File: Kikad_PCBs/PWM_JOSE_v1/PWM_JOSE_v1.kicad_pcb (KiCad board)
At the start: 2 copper layers, 197.2 x 153 mm, 528 parts, among them J1 signals, J3 AlimOut, J4 AlimIn, Q1 BC548, Q2 BC558, Q3 Q_NPN_CBE, U1 UC2844N, U2 PC817, U3 TL431

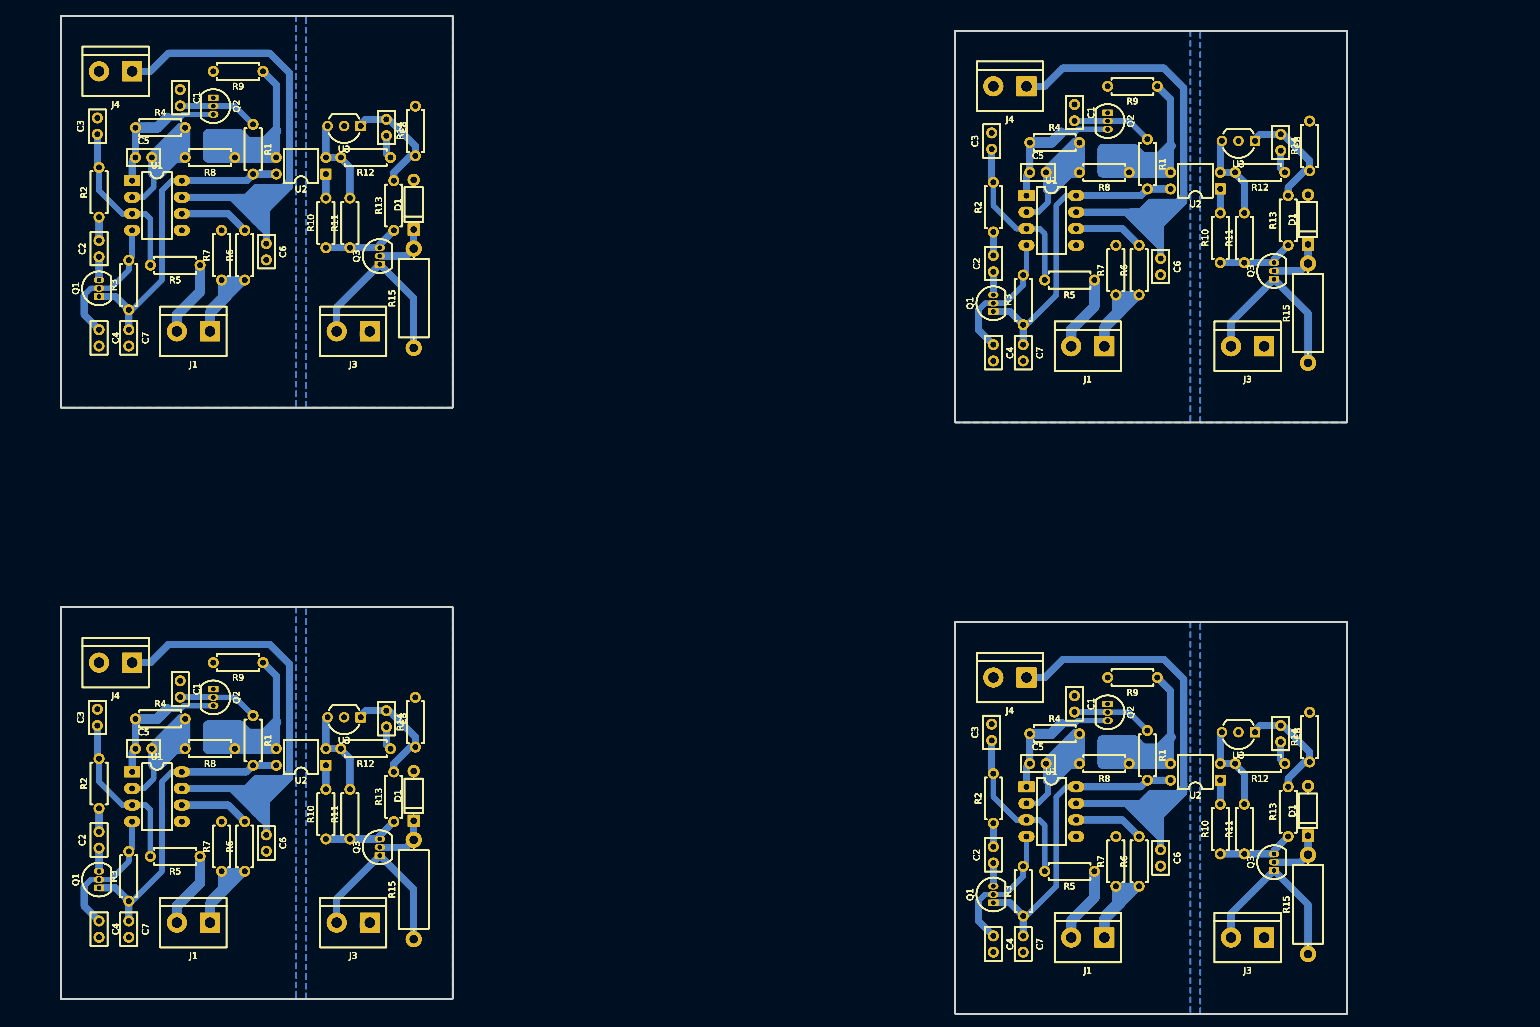
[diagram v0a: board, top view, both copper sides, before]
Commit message: modificacion de serigrafia del PCB y pdf serigrafi
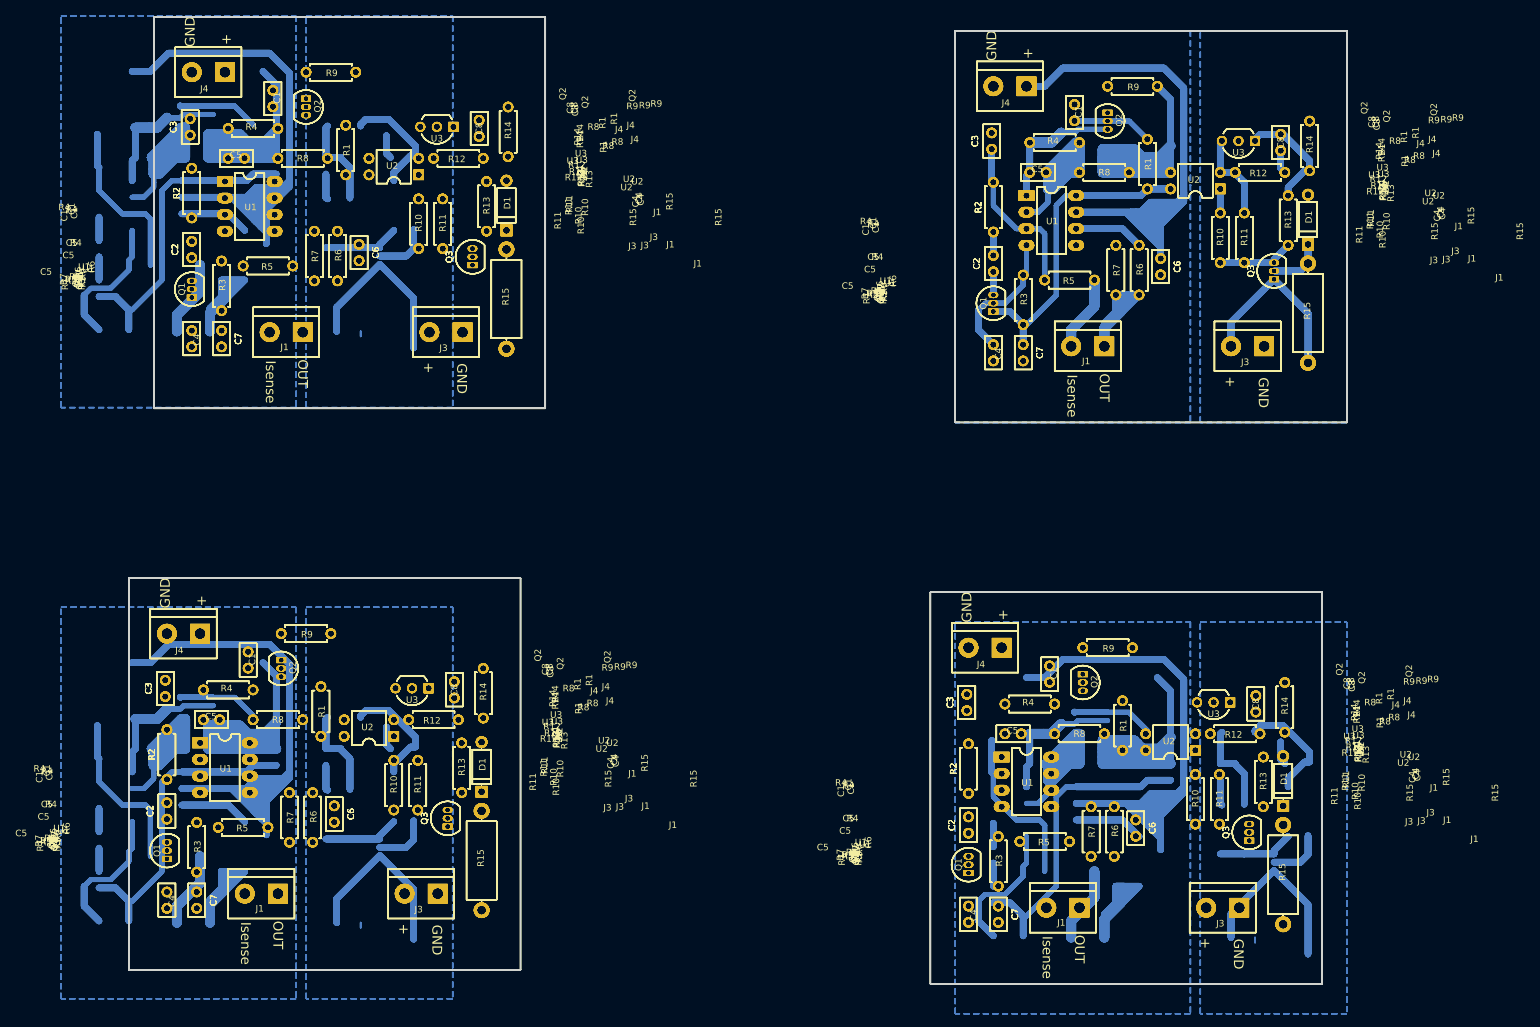
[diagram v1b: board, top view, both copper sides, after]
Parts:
- removed the C1 at (51.3, 126.0) (x4)
- removed the C1 at (51.3, 35.3) (x4)
- removed the C1 at (188.5, 128.3) (x4)
- removed the C2 at (38.9, 151.6) (x4)
- removed the C2 at (38.9, 61.0) (x4)
- removed the C2 at (176.0, 153.9) (x4)
- removed the C3 at (38.6, 132.8) (x4)
- removed the C3 at (38.6, 42.2) (x4)
- removed the C3 at (175.8, 135.1) (x4)
- removed the C4 at (38.9, 162.8) (x4)
- removed the C4 at (38.9, 72.1) (x4)
- removed the C4 at (176.0, 165.1) (x4)
- removed the C5 at (44.5, 136.4) (x4)
- removed the C5 at (44.5, 45.7) (x4)
- removed the C5 at (181.6, 138.7) (x4)
- removed the C6 at (64.5, 149.6) (x4)
- removed the C6 at (64.5, 58.9) (x4)
- removed the C6 at (201.7, 151.9) (x4)
- removed the C7 at (43.4, 162.8) (x4)
- removed the C7 at (43.4, 72.1) (x4)
- removed the C7 at (180.6, 165.1) (x4)
- removed the C8 at (82.9, 130.6) (x4)
- removed the C8 at (82.9, 39.9) (x4)
- removed the C8 at (220.1, 132.8) (x4)
- removed the D1 at (87.1, 147.4) (x4)
- removed the D1 at (87.1, 56.8) (x4)
- removed the D1 at (224.3, 149.7) (x4)
- removed the J1 at (55.9, 163.1) (x4)
- removed the J1 at (55.9, 72.4) (x4)
- removed the J1 at (193.0, 165.4) (x4)
- removed the J3 at (80.4, 163.1) (x4)
- removed the J3 at (80.4, 72.4) (x4)
- removed the J3 at (217.6, 165.4) (x4)
- removed the J4 at (43.9, 123.2) (x4)
- removed the J4 at (43.9, 32.5) (x4)
- removed the J4 at (181.1, 125.5) (x4)
- removed the Q1 at (38.9, 157.7) (x4)
- removed the Q1 at (38.9, 67.1) (x4)
- removed the Q1 at (176.0, 160.0) (x4)
- removed the Q2 at (56.4, 127.3) (x4)
- removed the Q2 at (56.4, 36.6) (x4)
- removed the Q2 at (193.5, 129.5) (x4)
- removed the Q3 at (81.9, 152.8) (x4)
- removed the Q3 at (81.9, 62.1) (x4)
- removed the Q3 at (219.1, 155.1) (x4)
- removed the R1 at (62.5, 131.3) (x4)
- removed the R1 at (62.5, 40.6) (x4)
- removed the R1 at (199.6, 133.6) (x4)
- removed the R10 at (73.7, 150.2) (x4)
- removed the R10 at (73.7, 59.6) (x4)
- removed the R10 at (210.8, 152.5) (x4)
- removed the R11 at (77.3, 150.2) (x4)
- removed the R11 at (77.3, 59.6) (x4)
- removed the R11 at (214.5, 152.5) (x4)
- removed the R12 at (83.6, 136.4) (x4)
- removed the R12 at (83.6, 45.7) (x4)
- removed the R12 at (220.7, 138.7) (x4)
- removed the R13 at (84.1, 147.6) (x4)
- removed the R13 at (84.1, 56.9) (x4)
- removed the R13 at (221.2, 149.9) (x4)
- removed the R14 at (87.4, 136.1) (x4)
- removed the R14 at (87.4, 45.5) (x4)
- removed the R14 at (224.5, 138.4) (x4)
- removed the R15 at (87.1, 165.6) (x4)
- removed the R15 at (87.1, 74.9) (x4)
- removed the R15 at (224.3, 167.9) (x4)
- removed the R2 at (38.9, 145.5) (x4)
- removed the R2 at (38.9, 54.9) (x4)
- removed the R2 at (176.0, 147.8) (x4)
- removed the R3 at (43.4, 159.8) (x4)
- removed the R3 at (43.4, 69.1) (x4)
- removed the R3 at (180.6, 162.1) (x4)
- removed the R4 at (44.5, 131.8) (x4)
- removed the R4 at (44.5, 41.1) (x4)
- removed the R4 at (181.6, 134.1) (x4)
- removed the R5 at (54.4, 152.9) (x4)
- removed the R5 at (54.4, 62.2) (x4)
- removed the R5 at (191.5, 155.2) (x4)
- removed the R6 at (61.2, 155.2) (x4)
- removed the R6 at (61.2, 64.5) (x4)
- removed the R6 at (198.4, 157.5) (x4)
- removed the R7 at (57.7, 155.2) (x4)
- removed the R7 at (57.7, 64.5) (x4)
- removed the R7 at (194.8, 157.5) (x4)
- removed the R8 at (59.7, 136.4) (x4)
- removed the R8 at (59.7, 45.7) (x4)
- removed the R8 at (196.8, 138.7) (x4)
- removed the R9 at (64.0, 123.2) (x4)
- removed the R9 at (64.0, 32.5) (x4)
- removed the R9 at (201.2, 125.5) (x4)
- removed the U1 at (43.9, 140.0) (x4)
- removed the U1 at (43.9, 49.3) (x4)
- removed the U1 at (181.1, 142.2) (x4)
- removed the U2 at (73.7, 138.9) (x4)
- removed the U2 at (73.7, 48.3) (x4)
- removed the U2 at (210.8, 141.2) (x4)
- removed the U3 at (79.0, 131.6) (x4)
- removed the U3 at (79.0, 40.9) (x4)
- removed the U3 at (216.2, 133.9) (x4)
- added C1 (x4): Css, Capacitors_THT:C_Disc_D5.0mm_W2.5mm_P2.50mm, F.Cu at (65.5, 35.4)
- added C1 (x4): Css, Capacitors_THT:C_Disc_D5.0mm_W2.5mm_P2.50mm, F.Cu at (184.7, 123.7)
- added C1 (x4): Css, Capacitors_THT:C_Disc_D5.0mm_W2.5mm_P2.50mm, F.Cu at (61.7, 121.5)
- added C2 (x4): Cramp, Capacitors_THT:C_Disc_D5.0mm_W2.5mm_P2.50mm, F.Cu at (53.1, 61.1)
- added C2 (x4): Cramp, Capacitors_THT:C_Disc_D5.0mm_W2.5mm_P2.50mm, F.Cu at (172.2, 149.4)
- added C2 (x4): Cramp, Capacitors_THT:C_Disc_D5.0mm_W2.5mm_P2.50mm, F.Cu at (49.3, 147.2)
- added C3 (x4): Ccsf, Capacitors_THT:C_Disc_D5.0mm_W2.5mm_P2.50mm, F.Cu at (52.8, 42.3)
- added C3 (x4): Ccsf, Capacitors_THT:C_Disc_D5.0mm_W2.5mm_P2.50mm, F.Cu at (172.0, 130.6)
- added C3 (x4): Ccsf, Capacitors_THT:C_Disc_D5.0mm_W2.5mm_P2.50mm, F.Cu at (49.0, 128.4)
- added C4 (x4): Cct, Capacitors_THT:C_Disc_D5.0mm_W2.5mm_P2.50mm, F.Cu at (53.1, 72.3)
- added C4 (x4): Cct, Capacitors_THT:C_Disc_D5.0mm_W2.5mm_P2.50mm, F.Cu at (172.2, 160.5)
- added C4 (x4): Cct, Capacitors_THT:C_Disc_D5.0mm_W2.5mm_P2.50mm, F.Cu at (49.3, 158.4)
- added C5 (x4): CcmpP, Capacitors_THT:C_Disc_D5.0mm_W2.5mm_P2.50mm, F.Cu at (58.7, 45.8)
- added C5 (x4): CcmpP, Capacitors_THT:C_Disc_D5.0mm_W2.5mm_P2.50mm, F.Cu at (177.8, 134.1)
- added C5 (x4): CcmpP, Capacitors_THT:C_Disc_D5.0mm_W2.5mm_P2.50mm, F.Cu at (54.9, 132.0)
- added C6 (x4): Cvcc, Capacitors_THT:C_Disc_D5.0mm_W2.5mm_P2.50mm, F.Cu at (78.7, 59.1)
- added C6 (x4): Cvcc, Capacitors_THT:C_Disc_D5.0mm_W2.5mm_P2.50mm, F.Cu at (197.9, 147.3)
- added C6 (x4): Cvcc, Capacitors_THT:C_Disc_D5.0mm_W2.5mm_P2.50mm, F.Cu at (74.9, 145.2)
- added C7 (x4): Cvref, Capacitors_THT:C_Disc_D5.0mm_W2.5mm_P2.50mm, F.Cu at (57.7, 72.3)
- added C7 (x4): Cvref, Capacitors_THT:C_Disc_D5.0mm_W2.5mm_P2.50mm, F.Cu at (176.8, 160.5)
- added C7 (x4): Cvref, Capacitors_THT:C_Disc_D5.0mm_W2.5mm_P2.50mm, F.Cu at (53.8, 158.4)
- added C8 (x4): CcmpZ, Capacitors_THT:C_Disc_D5.0mm_W2.5mm_P2.50mm, F.Cu at (97.2, 40.0)
- added C8 (x4): CcmpZ, Capacitors_THT:C_Disc_D5.0mm_W2.5mm_P2.50mm, F.Cu at (216.3, 128.3)
- added C8 (x4): CcmpZ, Capacitors_THT:C_Disc_D5.0mm_W2.5mm_P2.50mm, F.Cu at (93.3, 126.1)
- added D1 (x4): Zener, Diodes_THT:D_A-405_P7.62mm_Horizontal, F.Cu at (101.3, 56.9)
- added D1 (x4): Zener, Diodes_THT:D_A-405_P7.62mm_Horizontal, F.Cu at (220.5, 145.2)
- added D1 (x4): Zener, Diodes_THT:D_A-405_P7.62mm_Horizontal, F.Cu at (97.5, 143.0)
- added J1 (x4): signals, Connectors:bornier2, F.Cu at (70.1, 72.5)
- added J1 (x4): signals, Connectors:bornier2, F.Cu at (189.2, 160.8)
- added J1 (x4): signals, Connectors:bornier2, F.Cu at (66.3, 158.6)
- added J3 (x4): AlimOut, Connectors:bornier2, F.Cu at (94.6, 72.5)
- added J3 (x4): AlimOut, Connectors:bornier2, F.Cu at (213.7, 160.8)
- added J3 (x4): AlimOut, Connectors:bornier2, F.Cu at (90.8, 158.6)
- added J4 (x4): AlimIn, Connectors:bornier2, F.Cu at (58.2, 32.6)
- added J4 (x4): AlimIn, Connectors:bornier2, F.Cu at (177.3, 120.9)
- added J4 (x4): AlimIn, Connectors:bornier2, F.Cu at (54.4, 118.7)
- added Q1 (x4): BC548, TO_SOT_Packages_THT:TO-92_Inline_Narrow_Oval, F.Cu at (53.1, 67.2)
- added Q1 (x4): BC548, TO_SOT_Packages_THT:TO-92_Inline_Narrow_Oval, F.Cu at (172.2, 155.4)
- added Q1 (x4): BC548, TO_SOT_Packages_THT:TO-92_Inline_Narrow_Oval, F.Cu at (49.3, 153.3)
- added Q2 (x4): BC558, TO_SOT_Packages_THT:TO-92_Inline_Narrow_Oval, F.Cu at (70.6, 36.7)
- added Q2 (x4): BC558, TO_SOT_Packages_THT:TO-92_Inline_Narrow_Oval, F.Cu at (189.7, 125.0)
- added Q2 (x4): BC558, TO_SOT_Packages_THT:TO-92_Inline_Narrow_Oval, F.Cu at (66.8, 122.8)
- added Q3 (x4): Q_NPN_CBE, TO_SOT_Packages_THT:TO-92_Inline_Narrow_Oval, F.Cu at (96.1, 62.2)
- added Q3 (x4): Q_NPN_CBE, TO_SOT_Packages_THT:TO-92_Inline_Narrow_Oval, F.Cu at (215.3, 150.5)
- added Q3 (x4): Q_NPN_CBE, TO_SOT_Packages_THT:TO-92_Inline_Narrow_Oval, F.Cu at (92.3, 148.3)
- added R1 (x4): Rss, Resistors_THT:R_Axial_DIN0207_L6.3mm_D2.5mm_P7.62mm_Horizontal, F.Cu at (76.7, 40.8)
- added R1 (x4): Rss, Resistors_THT:R_Axial_DIN0207_L6.3mm_D2.5mm_P7.62mm_Horizontal, F.Cu at (195.8, 129.0)
- added R1 (x4): Rss, Resistors_THT:R_Axial_DIN0207_L6.3mm_D2.5mm_P7.62mm_Horizontal, F.Cu at (72.9, 126.9)
- added R10 (x4): Rled, Resistors_THT:R_Axial_DIN0207_L6.3mm_D2.5mm_P7.62mm_Horizontal, F.Cu at (87.9, 59.7)
- added R10 (x4): Rled, Resistors_THT:R_Axial_DIN0207_L6.3mm_D2.5mm_P7.62mm_Horizontal, F.Cu at (207.0, 148.0)
- added R10 (x4): Rled, Resistors_THT:R_Axial_DIN0207_L6.3mm_D2.5mm_P7.62mm_Horizontal, F.Cu at (84.1, 145.8)
- added R11 (x4): Rbias, Resistors_THT:R_Axial_DIN0207_L6.3mm_D2.5mm_P7.62mm_Horizontal, F.Cu at (91.6, 59.7)
- added R11 (x4): Rbias, Resistors_THT:R_Axial_DIN0207_L6.3mm_D2.5mm_P7.62mm_Horizontal, F.Cu at (210.7, 148.0)
- added R11 (x4): Rbias, Resistors_THT:R_Axial_DIN0207_L6.3mm_D2.5mm_P7.62mm_Horizontal, F.Cu at (87.8, 145.8)
- added R12 (x4): RcmpZ, Resistors_THT:R_Axial_DIN0207_L6.3mm_D2.5mm_P7.62mm_Horizontal, F.Cu at (97.8, 45.8)
- added R12 (x4): RcmpZ, Resistors_THT:R_Axial_DIN0207_L6.3mm_D2.5mm_P7.62mm_Horizontal, F.Cu at (216.9, 134.1)
- added R12 (x4): RcmpZ, Resistors_THT:R_Axial_DIN0207_L6.3mm_D2.5mm_P7.62mm_Horizontal, F.Cu at (94.0, 132.0)
- added R13 (x4): Rfbu, Resistors_THT:R_Axial_DIN0207_L6.3mm_D2.5mm_P7.62mm_Horizontal, F.Cu at (98.3, 57.0)
- added R13 (x4): Rfbu, Resistors_THT:R_Axial_DIN0207_L6.3mm_D2.5mm_P7.62mm_Horizontal, F.Cu at (217.4, 145.3)
- added R13 (x4): Rfbu, Resistors_THT:R_Axial_DIN0207_L6.3mm_D2.5mm_P7.62mm_Horizontal, F.Cu at (94.5, 143.1)
- added R14 (x4): Rfbb, Resistors_THT:R_Axial_DIN0207_L6.3mm_D2.5mm_P7.62mm_Horizontal, F.Cu at (101.6, 45.6)
- added R14 (x4): Rfbb, Resistors_THT:R_Axial_DIN0207_L6.3mm_D2.5mm_P7.62mm_Horizontal, F.Cu at (220.7, 133.9)
- added R14 (x4): Rfbb, Resistors_THT:R_Axial_DIN0207_L6.3mm_D2.5mm_P7.62mm_Horizontal, F.Cu at (97.8, 131.7)
- added R15 (x4): RZ, Resistors_THT:R_Axial_DIN0414_L11.9mm_D4.5mm_P15.24mm_Horizontal, F.Cu at (101.3, 75.1)
- added R15 (x4): RZ, Resistors_THT:R_Axial_DIN0414_L11.9mm_D4.5mm_P15.24mm_Horizontal, F.Cu at (220.5, 163.3)
- added R15 (x4): RZ, Resistors_THT:R_Axial_DIN0414_L11.9mm_D4.5mm_P15.24mm_Horizontal, F.Cu at (97.5, 161.2)
- added R2 (x4): Rramp, Resistors_THT:R_Axial_DIN0207_L6.3mm_D2.5mm_P7.62mm_Horizontal, F.Cu at (53.1, 55.0)
- added R2 (x4): Rramp, Resistors_THT:R_Axial_DIN0207_L6.3mm_D2.5mm_P7.62mm_Horizontal, F.Cu at (172.2, 143.3)
- added R2 (x4): Rramp, Resistors_THT:R_Axial_DIN0207_L6.3mm_D2.5mm_P7.62mm_Horizontal, F.Cu at (49.3, 141.1)
- added R3 (x4): Rrt, Resistors_THT:R_Axial_DIN0207_L6.3mm_D2.5mm_P7.62mm_Horizontal, F.Cu at (57.7, 69.2)
- added R3 (x4): Rrt, Resistors_THT:R_Axial_DIN0207_L6.3mm_D2.5mm_P7.62mm_Horizontal, F.Cu at (176.8, 157.5)
- added R3 (x4): Rrt, Resistors_THT:R_Axial_DIN0207_L6.3mm_D2.5mm_P7.62mm_Horizontal, F.Cu at (53.8, 155.3)
- added R4 (x4): RcmpP, Resistors_THT:R_Axial_DIN0207_L6.3mm_D2.5mm_P7.62mm_Horizontal, F.Cu at (58.7, 41.3)
- added R4 (x4): RcmpP, Resistors_THT:R_Axial_DIN0207_L6.3mm_D2.5mm_P7.62mm_Horizontal, F.Cu at (177.8, 129.5)
- added R4 (x4): RcmpP, Resistors_THT:R_Axial_DIN0207_L6.3mm_D2.5mm_P7.62mm_Horizontal, F.Cu at (54.9, 127.4)
- added R5 (x4): Rcsf, Resistors_THT:R_Axial_DIN0207_L6.3mm_D2.5mm_P7.62mm_Horizontal, F.Cu at (68.6, 62.4)
- added R5 (x4): Rcsf, Resistors_THT:R_Axial_DIN0207_L6.3mm_D2.5mm_P7.62mm_Horizontal, F.Cu at (187.7, 150.6)
- added R5 (x4): Rcsf, Resistors_THT:R_Axial_DIN0207_L6.3mm_D2.5mm_P7.62mm_Horizontal, F.Cu at (64.8, 148.5)
- added R6 (x4): Rg, Resistors_THT:R_Axial_DIN0207_L6.3mm_D2.5mm_P7.62mm_Horizontal, F.Cu at (75.4, 64.6)
- added R6 (x4): Rg, Resistors_THT:R_Axial_DIN0207_L6.3mm_D2.5mm_P7.62mm_Horizontal, F.Cu at (194.6, 152.9)
- added R6 (x4): Rg, Resistors_THT:R_Axial_DIN0207_L6.3mm_D2.5mm_P7.62mm_Horizontal, F.Cu at (71.6, 150.7)
- added R7 (x4): Rbled, Resistors_THT:R_Axial_DIN0207_L6.3mm_D2.5mm_P7.62mm_Horizontal, F.Cu at (71.9, 64.6)
- added R7 (x4): Rbled, Resistors_THT:R_Axial_DIN0207_L6.3mm_D2.5mm_P7.62mm_Horizontal, F.Cu at (191.0, 152.9)
- added R7 (x4): Rbled, Resistors_THT:R_Axial_DIN0207_L6.3mm_D2.5mm_P7.62mm_Horizontal, F.Cu at (68.1, 150.7)
- added R8 (x4): Rfbg, Resistors_THT:R_Axial_DIN0207_L6.3mm_D2.5mm_P7.62mm_Horizontal, F.Cu at (73.9, 45.8)
- added R8 (x4): Rfbg, Resistors_THT:R_Axial_DIN0207_L6.3mm_D2.5mm_P7.62mm_Horizontal, F.Cu at (193.0, 134.1)
- added R8 (x4): Rfbg, Resistors_THT:R_Axial_DIN0207_L6.3mm_D2.5mm_P7.62mm_Horizontal, F.Cu at (70.1, 132.0)
- added R9 (x4): Ropto, Resistors_THT:R_Axial_DIN0207_L6.3mm_D2.5mm_P7.62mm_Horizontal, F.Cu at (78.2, 32.6)
- added R9 (x4): Ropto, Resistors_THT:R_Axial_DIN0207_L6.3mm_D2.5mm_P7.62mm_Horizontal, F.Cu at (197.4, 120.9)
- added R9 (x4): Ropto, Resistors_THT:R_Axial_DIN0207_L6.3mm_D2.5mm_P7.62mm_Horizontal, F.Cu at (74.4, 118.7)
- added U1 (x4): UC2844N, Housings_DIP:DIP-8_W7.62mm_LongPads, F.Cu at (58.2, 49.4)
- added U1 (x4): UC2844N, Housings_DIP:DIP-8_W7.62mm_LongPads, F.Cu at (177.3, 137.7)
- added U1 (x4): UC2844N, Housings_DIP:DIP-8_W7.62mm_LongPads, F.Cu at (54.4, 135.5)
- added U2 (x4): PC817, Housings_DIP:DIP-4_W7.62mm, F.Cu at (87.9, 48.4)
- added U2 (x4): PC817, Housings_DIP:DIP-4_W7.62mm, F.Cu at (207.0, 136.7)
- added U2 (x4): PC817, Housings_DIP:DIP-4_W7.62mm, F.Cu at (84.1, 134.5)
- added U3 (x4): TL431, TO_SOT_Packages_THT:TO-92_Inline_Wide, F.Cu at (93.2, 41.0)
- added U3 (x4): TL431, TO_SOT_Packages_THT:TO-92_Inline_Wide, F.Cu at (212.3, 129.3)
- added U3 (x4): TL431, TO_SOT_Packages_THT:TO-92_Inline_Wide, F.Cu at (89.4, 127.1)
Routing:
- net (no net): track 0.00 -> 3579.9 mm
- net +12V: track 1737.9 -> 805.8 mm
- net Net-(R8-Pad1): track 987.2 -> 370.0 mm
- net Net-(C4-Pad1): track 624.7 -> 156.2 mm
- net GNDREF: track 0.00 -> 399.4 mm
- net Net-(J1-Pad1): track 470.9 -> 117.7 mm
- net +VDC: track 448.1 -> 112.0 mm
- net Net-(C5-Pad1): track 360.9 -> 90.2 mm
- net Net-(C7-Pad1): track 1024.7 -> 764.0 mm
- net Net-(C8-Pad1): track 284.5 -> 71.1 mm
- net Net-(C1-Pad2): track 262.6 -> 65.7 mm
- net Net-(C3-Pad1): track 550.8 -> 367.1 mm
- net Net-(C5-Pad2): track 631.6 -> 757.7 mm
- net GNDS: track 12.2 -> 129.5 mm
- net Net-(Q3-Pad3): track 189.1 -> 81.7 mm
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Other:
- board size 197.2 x 153 mm -> 186.8 x 148.3 mm
- board text added: "+"
- board text added: "GND"
- board text added: "Isense"
- board text added: "OUT"

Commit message: ultimo PCB con las serigrafias V2 (el qeu implemente y funcionaba)
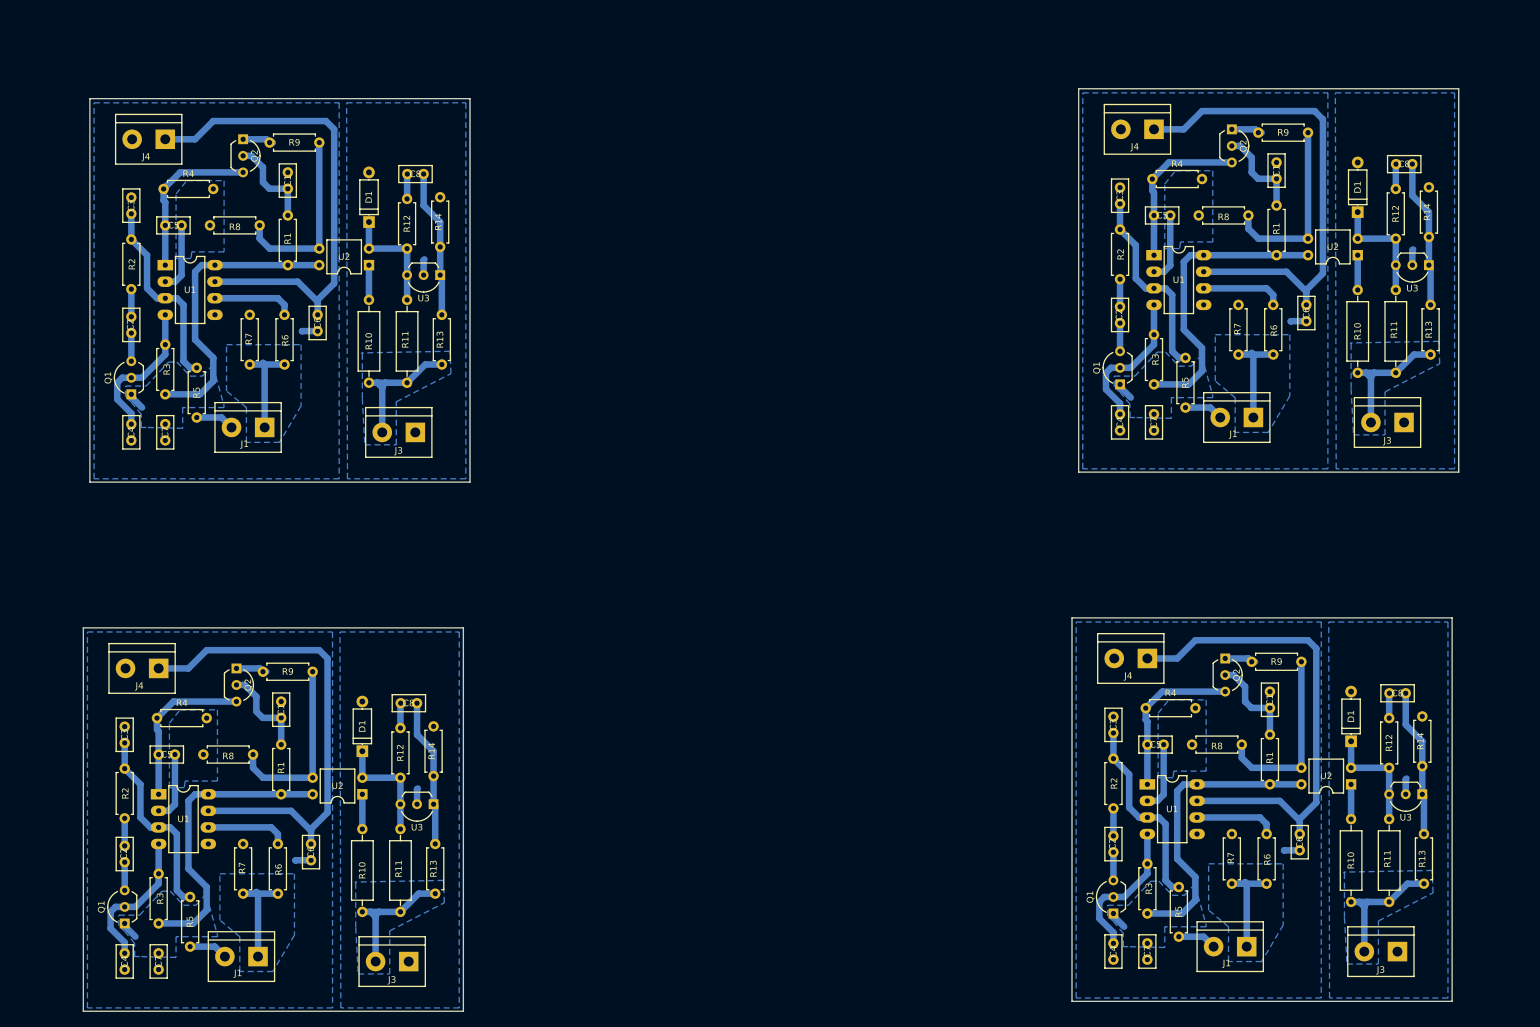
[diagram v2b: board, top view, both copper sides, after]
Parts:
- removed the C1 at (65.5, 35.4) (x4)
- removed the C1 at (184.7, 123.7) (x4)
- removed the C1 at (188.5, 37.6) (x4)
- removed the C1 at (61.7, 121.5) (x4)
- removed the C2 at (53.1, 61.1) (x4)
- removed the C2 at (172.2, 149.4) (x4)
- removed the C2 at (176.0, 63.2) (x4)
- removed the C2 at (49.3, 147.2) (x4)
- removed the C3 at (52.8, 42.3) (x4)
- removed the C3 at (172.0, 130.6) (x4)
- removed the C3 at (175.8, 44.5) (x4)
- removed the C3 at (49.0, 128.4) (x4)
- removed the C4 at (53.1, 72.3) (x4)
- removed the C4 at (172.2, 160.5) (x4)
- removed the C4 at (176.0, 74.4) (x4)
- removed the C4 at (49.3, 158.4) (x4)
- removed the C5 at (58.7, 45.8) (x4)
- removed the C5 at (177.8, 134.1) (x4)
- removed the C5 at (181.6, 48.0) (x4)
- removed the C5 at (54.9, 132.0) (x4)
- removed the C6 at (78.7, 59.1) (x4)
- removed the C6 at (197.9, 147.3) (x4)
- removed the C6 at (201.7, 61.2) (x4)
- removed the C6 at (74.9, 145.2) (x4)
- removed the C7 at (57.7, 72.3) (x4)
- removed the C7 at (176.8, 160.5) (x4)
- removed the C7 at (180.6, 74.4) (x4)
- removed the C7 at (53.8, 158.4) (x4)
- removed the C8 at (97.2, 40.0) (x4)
- removed the C8 at (216.3, 128.3) (x4)
- removed the C8 at (220.1, 42.2) (x4)
- removed the C8 at (93.3, 126.1) (x4)
- removed the D1 at (101.3, 56.9) (x4)
- removed the D1 at (220.5, 145.2) (x4)
- removed the D1 at (224.3, 59.1) (x4)
- removed the D1 at (97.5, 143.0) (x4)
- removed the J1 at (70.1, 72.5) (x4)
- removed the J1 at (189.2, 160.8) (x4)
- removed the J1 at (193.0, 74.7) (x4)
- removed the J1 at (66.3, 158.6) (x4)
- removed the J3 at (94.6, 72.5) (x4)
- removed the J3 at (213.7, 160.8) (x4)
- removed the J3 at (217.6, 74.7) (x4)
- removed the J3 at (90.8, 158.6) (x4)
- removed the J4 at (58.2, 32.6) (x4)
- removed the J4 at (177.3, 120.9) (x4)
- removed the J4 at (181.1, 34.8) (x4)
- removed the J4 at (54.4, 118.7) (x4)
- removed the Q1 at (53.1, 67.2) (x4)
- removed the Q1 at (172.2, 155.4) (x4)
- removed the Q1 at (176.0, 69.3) (x4)
- removed the Q1 at (49.3, 153.3) (x4)
- removed the Q2 at (70.6, 36.7) (x4)
- removed the Q2 at (189.7, 125.0) (x4)
- removed the Q2 at (193.5, 38.9) (x4)
- removed the Q2 at (66.8, 122.8) (x4)
- removed Q3 (x16): Q_NPN_CBE, TO_SOT_Packages_THT:TO-92_Inline_Narrow_Oval
- removed the R1 at (76.7, 40.8) (x4)
- removed the R1 at (195.8, 129.0) (x4)
- removed the R1 at (199.6, 42.9) (x4)
- removed the R1 at (72.9, 126.9) (x4)
- removed the R10 at (87.9, 59.7) (x4)
- removed the R10 at (207.0, 148.0) (x4)
- removed the R10 at (210.8, 61.8) (x4)
- removed the R10 at (84.1, 145.8) (x4)
- removed the R11 at (91.6, 59.7) (x4)
- removed the R11 at (210.7, 148.0) (x4)
- removed the R11 at (214.5, 61.8) (x4)
- removed the R11 at (87.8, 145.8) (x4)
- removed the R12 at (97.8, 45.8) (x4)
- removed the R12 at (216.9, 134.1) (x4)
- removed the R12 at (220.7, 48.0) (x4)
- removed the R12 at (94.0, 132.0) (x4)
- removed the R13 at (98.3, 57.0) (x4)
- removed the R13 at (217.4, 145.3) (x4)
- removed the R13 at (221.2, 59.2) (x4)
- removed the R13 at (94.5, 143.1) (x4)
- removed the R14 at (101.6, 45.6) (x4)
- removed the R14 at (220.7, 133.9) (x4)
- removed the R14 at (224.5, 47.8) (x4)
- removed the R14 at (97.8, 131.7) (x4)
- removed R15 (x16): RZ, Resistors_THT:R_Axial_DIN0414_L11.9mm_D4.5mm_P15.24mm_Horizontal
- removed the R2 at (53.1, 55.0) (x4)
- removed the R2 at (172.2, 143.3) (x4)
- removed the R2 at (176.0, 57.1) (x4)
- removed the R2 at (49.3, 141.1) (x4)
- removed the R3 at (57.7, 69.2) (x4)
- removed the R3 at (176.8, 157.5) (x4)
- removed the R3 at (180.6, 71.4) (x4)
- removed the R3 at (53.8, 155.3) (x4)
- removed the R4 at (58.7, 41.3) (x4)
- removed the R4 at (177.8, 129.5) (x4)
- removed the R4 at (181.6, 43.4) (x4)
- removed the R4 at (54.9, 127.4) (x4)
- removed the R5 at (68.6, 62.4) (x4)
- removed the R5 at (187.7, 150.6) (x4)
- removed the R5 at (191.5, 64.5) (x4)
- removed the R5 at (64.8, 148.5) (x4)
- removed the R6 at (75.4, 64.6) (x4)
- removed the R6 at (194.6, 152.9) (x4)
- removed the R6 at (198.4, 66.8) (x4)
- removed the R6 at (71.6, 150.7) (x4)
- removed the R7 at (71.9, 64.6) (x4)
- removed the R7 at (191.0, 152.9) (x4)
- removed the R7 at (194.8, 66.8) (x4)
- removed the R7 at (68.1, 150.7) (x4)
- removed the R8 at (73.9, 45.8) (x4)
- removed the R8 at (193.0, 134.1) (x4)
- removed the R8 at (196.8, 48.0) (x4)
- removed the R8 at (70.1, 132.0) (x4)
- removed the R9 at (78.2, 32.6) (x4)
- removed the R9 at (197.4, 120.9) (x4)
- removed the R9 at (201.2, 34.8) (x4)
- removed the R9 at (74.4, 118.7) (x4)
- removed the U1 at (58.2, 49.4) (x4)
- removed the U1 at (177.3, 137.7) (x4)
- removed the U1 at (181.1, 51.6) (x4)
- removed the U1 at (54.4, 135.5) (x4)
- removed the U2 at (87.9, 48.4) (x4)
- removed the U2 at (207.0, 136.7) (x4)
- removed the U2 at (210.8, 50.5) (x4)
- removed the U2 at (84.1, 134.5) (x4)
- removed the U3 at (93.2, 41.0) (x4)
- removed the U3 at (212.3, 129.3) (x4)
- removed the U3 at (216.2, 43.2) (x4)
- removed the U3 at (89.4, 127.1) (x4)
- added C1: Css, Capacitors_THT:C_Disc_D5.0mm_W2.5mm_P2.50mm, F.Cu at (219.5, 46.5)
- added C1: Css, Capacitors_THT:C_Disc_D5.0mm_W2.5mm_P2.50mm, F.Cu at (218.4, 127.6)
- added C1: Css, Capacitors_THT:C_Disc_D5.0mm_W2.5mm_P2.50mm, F.Cu at (66.8, 129.2)
- added C1: Css, Capacitors_THT:C_Disc_D5.0mm_W2.5mm_P2.50mm, F.Cu at (67.8, 48.0)
- added C2: Cramp, Capacitors_THT:C_Disc_D5.0mm_W2.5mm_P2.50mm, F.Cu at (195.5, 71.1)
- added C2: Cramp, Capacitors_THT:C_Disc_D5.0mm_W2.5mm_P2.50mm, F.Cu at (194.4, 152.3)
- added C2: Cramp, Capacitors_THT:C_Disc_D5.0mm_W2.5mm_P2.50mm, F.Cu at (42.8, 153.8)
- added C2: Cramp, Capacitors_THT:C_Disc_D5.0mm_W2.5mm_P2.50mm, F.Cu at (43.8, 72.6)
- added C3: Ccsf, Capacitors_THT:C_Disc_D5.0mm_W2.5mm_P2.50mm, F.Cu at (195.5, 52.8)
- added C3: Ccsf, Capacitors_THT:C_Disc_D5.0mm_W2.5mm_P2.50mm, F.Cu at (194.4, 134.0)
- added C3: Ccsf, Capacitors_THT:C_Disc_D5.0mm_W2.5mm_P2.50mm, F.Cu at (42.8, 135.5)
- added C3: Ccsf, Capacitors_THT:C_Disc_D5.0mm_W2.5mm_P2.50mm, F.Cu at (43.8, 54.4)
- added C4: Cct, Capacitors_THT:C_Disc_D5.0mm_W2.5mm_P2.50mm, F.Cu at (195.5, 85.1)
- added C4: Cct, Capacitors_THT:C_Disc_D5.0mm_W2.5mm_P2.50mm, F.Cu at (194.4, 166.2)
- added C4: Cct, Capacitors_THT:C_Disc_D5.0mm_W2.5mm_P2.50mm, F.Cu at (42.8, 167.8)
- added C4: Cct, Capacitors_THT:C_Disc_D5.0mm_W2.5mm_P2.50mm, F.Cu at (43.8, 86.6)
- added C5: CcmpP, Capacitors_THT:C_Disc_D5.0mm_W2.5mm_P2.50mm, F.Cu at (200.7, 54.6)
- added C5: CcmpP, Capacitors_THT:C_Disc_D5.0mm_W2.5mm_P2.50mm, F.Cu at (199.6, 135.8)
- added C5: CcmpP, Capacitors_THT:C_Disc_D5.0mm_W2.5mm_P2.50mm, F.Cu at (48.0, 137.3)
- added C5: CcmpP, Capacitors_THT:C_Disc_D5.0mm_W2.5mm_P2.50mm, F.Cu at (49.0, 56.1)
- added C6: Cvcc, Capacitors_THT:C_Disc_D5.0mm_W2.5mm_P2.50mm, F.Cu at (224.0, 68.3)
- added C6: Cvcc, Capacitors_THT:C_Disc_D5.0mm_W2.5mm_P2.50mm, F.Cu at (223.0, 149.5)
- added C6: Cvcc, Capacitors_THT:C_Disc_D5.0mm_W2.5mm_P2.50mm, F.Cu at (71.4, 151.0)
- added C6: Cvcc, Capacitors_THT:C_Disc_D5.0mm_W2.5mm_P2.50mm, F.Cu at (72.4, 69.8)
- added C7: Cvref, Capacitors_THT:C_Disc_D5.0mm_W2.5mm_P2.50mm, F.Cu at (200.7, 85.1)
- added C7: Cvref, Capacitors_THT:C_Disc_D5.0mm_W2.5mm_P2.50mm, F.Cu at (199.6, 166.2)
- added C7: Cvref, Capacitors_THT:C_Disc_D5.0mm_W2.5mm_P2.50mm, F.Cu at (48.0, 167.8)
- added C7: Cvref, Capacitors_THT:C_Disc_D5.0mm_W2.5mm_P2.50mm, F.Cu at (49.0, 86.6)
- added C8: CcmpZ, Capacitors_THT:C_Disc_D5.0mm_W2.5mm_P2.50mm, F.Cu at (240.3, 46.7)
- added C8: CcmpZ, Capacitors_THT:C_Disc_D5.0mm_W2.5mm_P2.50mm, F.Cu at (239.3, 127.9)
- added C8: CcmpZ, Capacitors_THT:C_Disc_D5.0mm_W2.5mm_P2.50mm, F.Cu at (87.6, 129.4)
- added C8: CcmpZ, Capacitors_THT:C_Disc_D5.0mm_W2.5mm_P2.50mm, F.Cu at (88.6, 48.3)
- added D1: Zener, Diodes_THT:D_A-405_P7.62mm_Horizontal, F.Cu at (231.9, 54.1)
- added D1: Zener, Diodes_THT:D_A-405_P7.62mm_Horizontal, F.Cu at (230.9, 135.3)
- added D1: Zener, Diodes_THT:D_A-405_P7.62mm_Horizontal, F.Cu at (79.2, 136.8)
- added D1: Zener, Diodes_THT:D_A-405_P7.62mm_Horizontal, F.Cu at (80.3, 55.6)
- added J1: signals, Connectors:bornier2, F.Cu at (215.9, 85.6)
- added J1: signals, Connectors:bornier2, F.Cu at (214.9, 166.8)
- added J1: signals, Connectors:bornier2, F.Cu at (63.2, 168.3)
- added J1: signals, Connectors:bornier2, F.Cu at (64.3, 87.1)
- added J3: AlimOut, Connectors:bornier2, F.Cu at (239.0, 86.4)
- added J3: AlimOut, Connectors:bornier2, F.Cu at (238.0, 167.5)
- added J3: AlimOut, Connectors:bornier2, F.Cu at (86.4, 169.0)
- added J3: AlimOut, Connectors:bornier2, F.Cu at (87.4, 87.9)
- added J4: AlimIn, Connectors:bornier2, F.Cu at (200.7, 41.4)
- added J4: AlimIn, Connectors:bornier2, F.Cu at (199.6, 122.6)
- added J4: AlimIn, Connectors:bornier2, F.Cu at (48.0, 124.1)
- added J4: AlimIn, Connectors:bornier2, F.Cu at (49.0, 42.9)
- added Q1: BC548, TO_SOT_Packages_THT:TO-92_Inline_Wide, F.Cu at (195.5, 80.5)
- added Q1: BC548, TO_SOT_Packages_THT:TO-92_Inline_Wide, F.Cu at (194.4, 161.7)
- added Q1: BC548, TO_SOT_Packages_THT:TO-92_Inline_Wide, F.Cu at (42.8, 163.2)
- added Q1: BC548, TO_SOT_Packages_THT:TO-92_Inline_Wide, F.Cu at (43.8, 82.0)
- added Q2: BC558, TO_SOT_Packages_THT:TO-92_Inline_Wide, F.Cu at (212.6, 41.4)
- added Q2: BC558, TO_SOT_Packages_THT:TO-92_Inline_Wide, F.Cu at (211.6, 122.6)
- added Q2: BC558, TO_SOT_Packages_THT:TO-92_Inline_Wide, F.Cu at (59.9, 124.1)
- added Q2: BC558, TO_SOT_Packages_THT:TO-92_Inline_Wide, F.Cu at (61.0, 42.9)
- added R1: Rss, Resistors_THT:R_Axial_DIN0207_L6.3mm_D2.5mm_P7.62mm_Horizontal, F.Cu at (219.5, 53.1)
- added R1: Rss, Resistors_THT:R_Axial_DIN0207_L6.3mm_D2.5mm_P7.62mm_Horizontal, F.Cu at (218.4, 134.2)
- added R1: Rss, Resistors_THT:R_Axial_DIN0207_L6.3mm_D2.5mm_P7.62mm_Horizontal, F.Cu at (66.8, 135.8)
- added R1: Rss, Resistors_THT:R_Axial_DIN0207_L6.3mm_D2.5mm_P7.62mm_Horizontal, F.Cu at (67.8, 54.6)
- added R10: Rled, Resistors_THT:R_Axial_DIN0309_L9.0mm_D3.2mm_P12.70mm_Horizontal, F.Cu at (231.9, 78.7)
- added R10: Rled, Resistors_THT:R_Axial_DIN0309_L9.0mm_D3.2mm_P12.70mm_Horizontal, F.Cu at (230.9, 159.9)
- added R10: Rled, Resistors_THT:R_Axial_DIN0309_L9.0mm_D3.2mm_P12.70mm_Horizontal, F.Cu at (79.2, 161.4)
- added R10: Rled, Resistors_THT:R_Axial_DIN0309_L9.0mm_D3.2mm_P12.70mm_Horizontal, F.Cu at (80.3, 80.3)
- added R11: Rbias, Resistors_THT:R_Axial_DIN0309_L9.0mm_D3.2mm_P12.70mm_Horizontal, F.Cu at (237.7, 78.7)
- added R11: Rbias, Resistors_THT:R_Axial_DIN0309_L9.0mm_D3.2mm_P12.70mm_Horizontal, F.Cu at (236.7, 159.9)
- added R11: Rbias, Resistors_THT:R_Axial_DIN0309_L9.0mm_D3.2mm_P12.70mm_Horizontal, F.Cu at (85.1, 161.4)
- added R11: Rbias, Resistors_THT:R_Axial_DIN0309_L9.0mm_D3.2mm_P12.70mm_Horizontal, F.Cu at (86.1, 80.3)
- added R12: RcmpZ, Resistors_THT:R_Axial_DIN0207_L6.3mm_D2.5mm_P7.62mm_Horizontal, F.Cu at (237.7, 50.5)
- added R12: RcmpZ, Resistors_THT:R_Axial_DIN0207_L6.3mm_D2.5mm_P7.62mm_Horizontal, F.Cu at (236.7, 131.7)
- added R12: RcmpZ, Resistors_THT:R_Axial_DIN0207_L6.3mm_D2.5mm_P7.62mm_Horizontal, F.Cu at (85.1, 133.2)
- added R12: RcmpZ, Resistors_THT:R_Axial_DIN0207_L6.3mm_D2.5mm_P7.62mm_Horizontal, F.Cu at (86.1, 52.1)
- added R13: Rfbu, Resistors_THT:R_Axial_DIN0207_L6.3mm_D2.5mm_P7.62mm_Horizontal, F.Cu at (243.1, 75.9)
- added R13: Rfbu, Resistors_THT:R_Axial_DIN0207_L6.3mm_D2.5mm_P7.62mm_Horizontal, F.Cu at (242.1, 157.1)
- added R13: Rfbu, Resistors_THT:R_Axial_DIN0207_L6.3mm_D2.5mm_P7.62mm_Horizontal, F.Cu at (90.4, 158.6)
- added R13: Rfbu, Resistors_THT:R_Axial_DIN0207_L6.3mm_D2.5mm_P7.62mm_Horizontal, F.Cu at (91.4, 77.5)
- added R14: Rfbb, Resistors_THT:R_Axial_DIN0207_L6.3mm_D2.5mm_P7.62mm_Horizontal, F.Cu at (242.8, 57.9)
- added R14: Rfbb, Resistors_THT:R_Axial_DIN0207_L6.3mm_D2.5mm_P7.62mm_Horizontal, F.Cu at (241.8, 139.1)
- added R14: Rfbb, Resistors_THT:R_Axial_DIN0207_L6.3mm_D2.5mm_P7.62mm_Horizontal, F.Cu at (90.2, 140.6)
- added R14: Rfbb, Resistors_THT:R_Axial_DIN0207_L6.3mm_D2.5mm_P7.62mm_Horizontal, F.Cu at (91.2, 59.4)
- added R2: Rramp, Resistors_THT:R_Axial_DIN0207_L6.3mm_D2.5mm_P7.62mm_Horizontal, F.Cu at (195.5, 64.4)
- added R2: Rramp, Resistors_THT:R_Axial_DIN0207_L6.3mm_D2.5mm_P7.62mm_Horizontal, F.Cu at (194.4, 145.5)
- added R2: Rramp, Resistors_THT:R_Axial_DIN0207_L6.3mm_D2.5mm_P7.62mm_Horizontal, F.Cu at (42.8, 147.1)
- added R2: Rramp, Resistors_THT:R_Axial_DIN0207_L6.3mm_D2.5mm_P7.62mm_Horizontal, F.Cu at (43.8, 65.9)
- added R3: Rrt, Resistors_THT:R_Axial_DIN0207_L6.3mm_D2.5mm_P7.62mm_Horizontal, F.Cu at (200.7, 80.5)
- added R3: Rrt, Resistors_THT:R_Axial_DIN0207_L6.3mm_D2.5mm_P7.62mm_Horizontal, F.Cu at (199.6, 161.7)
- added R3: Rrt, Resistors_THT:R_Axial_DIN0207_L6.3mm_D2.5mm_P7.62mm_Horizontal, F.Cu at (48.0, 163.2)
- added R3: Rrt, Resistors_THT:R_Axial_DIN0207_L6.3mm_D2.5mm_P7.62mm_Horizontal, F.Cu at (49.0, 82.0)
- added R4: RcmpP, Resistors_THT:R_Axial_DIN0207_L6.3mm_D2.5mm_P7.62mm_Horizontal, F.Cu at (200.4, 49.0)
- added R4: RcmpP, Resistors_THT:R_Axial_DIN0207_L6.3mm_D2.5mm_P7.62mm_Horizontal, F.Cu at (199.4, 130.2)
- added R4: RcmpP, Resistors_THT:R_Axial_DIN0207_L6.3mm_D2.5mm_P7.62mm_Horizontal, F.Cu at (47.8, 131.7)
- added R4: RcmpP, Resistors_THT:R_Axial_DIN0207_L6.3mm_D2.5mm_P7.62mm_Horizontal, F.Cu at (48.8, 50.5)
- added R5: Rcsf, Resistors_THT:R_Axial_DIN0207_L6.3mm_D2.5mm_P7.62mm_Horizontal, F.Cu at (205.5, 84.1)
- added R5: Rcsf, Resistors_THT:R_Axial_DIN0207_L6.3mm_D2.5mm_P7.62mm_Horizontal, F.Cu at (204.5, 165.2)
- added R5: Rcsf, Resistors_THT:R_Axial_DIN0207_L6.3mm_D2.5mm_P7.62mm_Horizontal, F.Cu at (52.8, 166.8)
- added R5: Rcsf, Resistors_THT:R_Axial_DIN0207_L6.3mm_D2.5mm_P7.62mm_Horizontal, F.Cu at (53.8, 85.6)
- added R6: Rg, Resistors_THT:R_Axial_DIN0207_L6.3mm_D2.5mm_P7.62mm_Horizontal, F.Cu at (218.9, 75.9)
- added R6: Rg, Resistors_THT:R_Axial_DIN0207_L6.3mm_D2.5mm_P7.62mm_Horizontal, F.Cu at (217.9, 157.1)
- added R6: Rg, Resistors_THT:R_Axial_DIN0207_L6.3mm_D2.5mm_P7.62mm_Horizontal, F.Cu at (66.3, 158.6)
- added R6: Rg, Resistors_THT:R_Axial_DIN0207_L6.3mm_D2.5mm_P7.62mm_Horizontal, F.Cu at (67.3, 77.5)
- added R7: Rbled, Resistors_THT:R_Axial_DIN0207_L6.3mm_D2.5mm_P7.62mm_Horizontal, F.Cu at (213.6, 75.9)
- added R7: Rbled, Resistors_THT:R_Axial_DIN0207_L6.3mm_D2.5mm_P7.62mm_Horizontal, F.Cu at (212.6, 157.1)
- added R7: Rbled, Resistors_THT:R_Axial_DIN0207_L6.3mm_D2.5mm_P7.62mm_Horizontal, F.Cu at (61.0, 158.6)
- added R7: Rbled, Resistors_THT:R_Axial_DIN0207_L6.3mm_D2.5mm_P7.62mm_Horizontal, F.Cu at (62.0, 77.5)
- added R8: Rfbg, Resistors_THT:R_Axial_DIN0207_L6.3mm_D2.5mm_P7.62mm_Horizontal, F.Cu at (215.1, 54.6)
- added R8: Rfbg, Resistors_THT:R_Axial_DIN0207_L6.3mm_D2.5mm_P7.62mm_Horizontal, F.Cu at (214.1, 135.8)
- added R8: Rfbg, Resistors_THT:R_Axial_DIN0207_L6.3mm_D2.5mm_P7.62mm_Horizontal, F.Cu at (62.5, 137.3)
- added R8: Rfbg, Resistors_THT:R_Axial_DIN0207_L6.3mm_D2.5mm_P7.62mm_Horizontal, F.Cu at (63.5, 56.1)
- added R9: Ropto, Resistors_THT:R_Axial_DIN0207_L6.3mm_D2.5mm_P7.62mm_Horizontal, F.Cu at (224.3, 41.9)
- added R9: Ropto, Resistors_THT:R_Axial_DIN0207_L6.3mm_D2.5mm_P7.62mm_Horizontal, F.Cu at (223.3, 123.1)
- added R9: Ropto, Resistors_THT:R_Axial_DIN0207_L6.3mm_D2.5mm_P7.62mm_Horizontal, F.Cu at (71.6, 124.6)
- added R9: Ropto, Resistors_THT:R_Axial_DIN0207_L6.3mm_D2.5mm_P7.62mm_Horizontal, F.Cu at (72.6, 43.4)
- added U1: UC2844N, Housings_DIP:DIP-8_W7.62mm_LongPads, F.Cu at (200.7, 60.7)
- added U1: UC2844N, Housings_DIP:DIP-8_W7.62mm_LongPads, F.Cu at (199.6, 141.9)
- added U1: UC2844N, Housings_DIP:DIP-8_W7.62mm_LongPads, F.Cu at (48.0, 143.4)
- added U1: UC2844N, Housings_DIP:DIP-8_W7.62mm_LongPads, F.Cu at (49.0, 62.2)
- added U2: PC817, Housings_DIP:DIP-4_W7.62mm, F.Cu at (231.9, 60.7)
- added U2: PC817, Housings_DIP:DIP-4_W7.62mm, F.Cu at (230.9, 141.9)
- added U2: PC817, Housings_DIP:DIP-4_W7.62mm, F.Cu at (79.2, 143.4)
- added U2: PC817, Housings_DIP:DIP-4_W7.62mm, F.Cu at (80.3, 62.2)
- added U3: TL431, TO_SOT_Packages_THT:TO-92_Inline_Wide, F.Cu at (242.8, 62.2)
- added U3: TL431, TO_SOT_Packages_THT:TO-92_Inline_Wide, F.Cu at (241.8, 143.4)
- added U3: TL431, TO_SOT_Packages_THT:TO-92_Inline_Wide, F.Cu at (90.2, 144.9)
- added U3: TL431, TO_SOT_Packages_THT:TO-92_Inline_Wide, F.Cu at (91.2, 63.8)
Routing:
- net (no net): track 3579.9 -> 0.00 mm
- net Net-(C5-Pad2): track 757.7 -> 42.3 mm
- net Net-(C7-Pad1): track 764.0 -> 193.3 mm
- net +12V: track 805.8 -> 296.4 mm
- net GNDREF: track 399.4 -> 32.4 mm
- net Net-(R6-Pad2): track 384.3 -> 50.5 mm
- net Net-(R8-Pad1): track 370.0 -> 112.3 mm
- net Net-(C3-Pad1): track 367.1 -> 120.6 mm
- net Net-(R11-Pad2): track 128.6 -> 0.00 mm
- net GNDS: track 129.5 -> 9.86 mm
- net Net-(J1-Pad2): track 120.4 -> 24.9 mm
- net Net-(Q3-Pad3): track 81.7 -> 0.00 mm
- net Net-(R10-Pad2): track 88.7 -> 21.3 mm
- net Net-(C4-Pad1): track 156.2 -> 90.0 mm
- net Net-(J1-Pad1): track 117.7 -> 62.4 mm
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- added copper zone on B.Cu, net +VDC
- added copper zone on B.Cu, net Net-(C5-Pad2)
- added copper zone on B.Cu, net Net-(C7-Pad1)
- added copper zone on B.Cu, net Net-(J1-Pad1)
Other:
- board size 186.8 x 148.3 mm -> 210.9 x 141.5 mm
- board text added: "ISns"
- board text removed: "Isense"
